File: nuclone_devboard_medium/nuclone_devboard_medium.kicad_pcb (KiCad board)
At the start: 2 copper layers, 50 x 76.2 mm, 40 parts, among them J1 JTAG_2X05, J2 TYPE-C-31-M-12, J3 nuclone_medium_left, J4 nuclone_medium_right, J5 Conn_02x06_Odd_Even, SW1 RESET, SW2 Bootloader, U1 MCP1702-3.3V, U2 TPESD0504C6

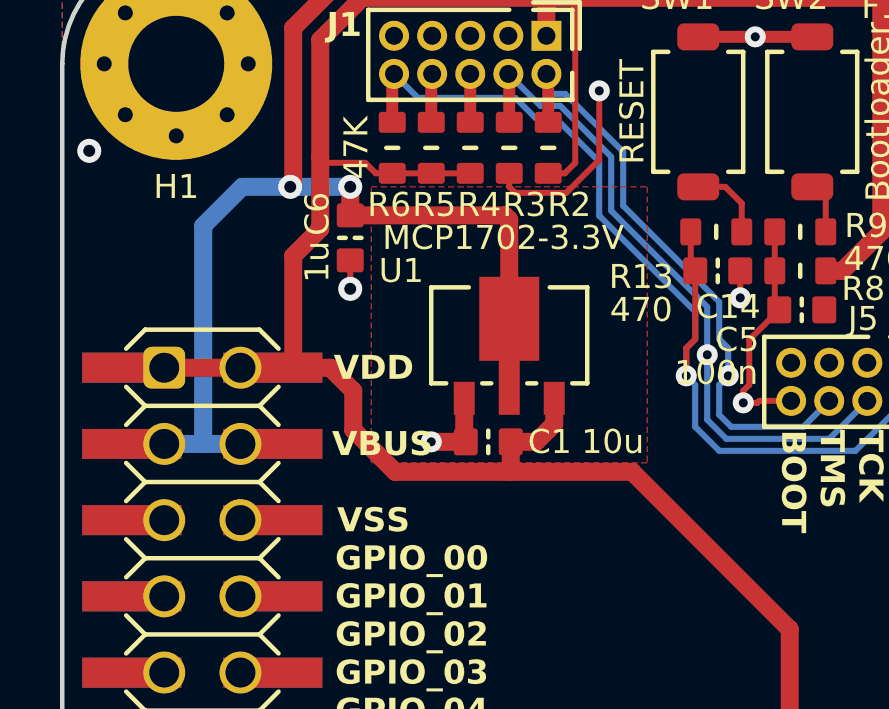
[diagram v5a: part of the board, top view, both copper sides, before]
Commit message: updated regulator cooling
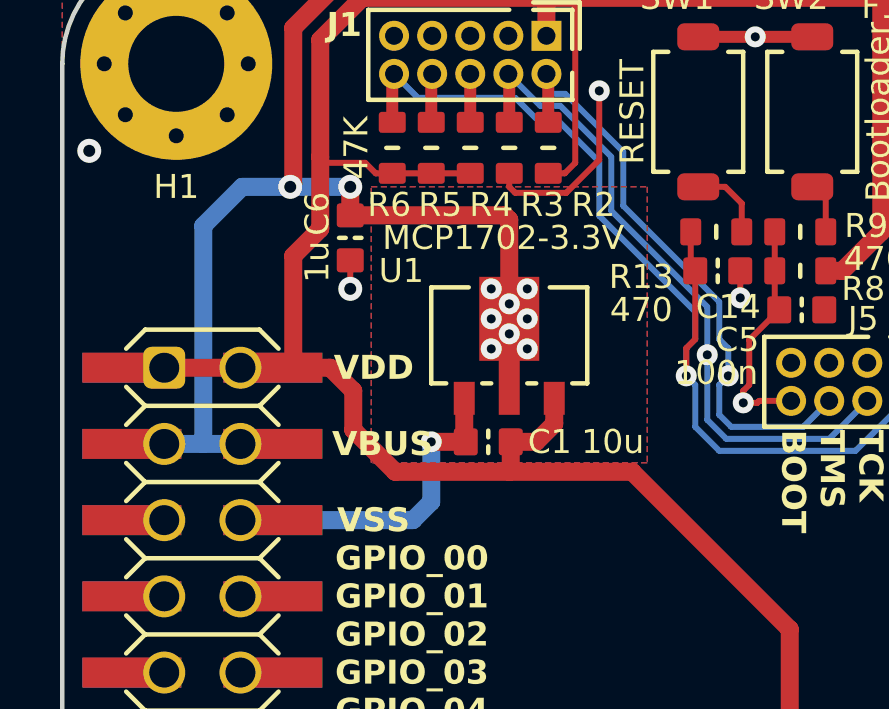
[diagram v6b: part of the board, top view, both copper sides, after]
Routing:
- net /VSS: track 36.0 -> 44.6 mm
- net /VBUS: track 89.4 -> 91.2 mm, vias 6 -> 14
- added copper zone on B.Cu, net /VBUS
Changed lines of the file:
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@@
     (property "ki_keywords" "R res resistor")
     (attr smd)
-    (fp_text reference "R3" (at 1.9 -0.5) (layer "F.SilkS")
+    (fp_text reference "R3" (at 1.9 -1.1) (layer "F.SilkS")
         (effects (font (size 0.8 0.8) (thickness 0.15)))
     )
@@
     (property "ki_keywords" "R res resistor")
     (attr smd)
-    (fp_text reference "R5" (at 1.9 -0.1) (layer "F.SilkS")
+    (fp_text reference "R5" (at 1.9 -0.3) (layer "F.SilkS")
         (effects (font (size 0.8 0.8) (thickness 0.15)))
     )
@@
     (property "ki_keywords" "R res resistor")
     (attr smd)
-    (fp_text reference "R2" (at 1.9 -0.7) (layer "F.SilkS")
+    (fp_text reference "R2" (at 1.9 -1.5) (layer "F.SilkS")
         (effects (font (size 0.8 0.8) (thickness 0.15)))
     )
@@
     (property "ki_keywords" "R res resistor")
     (attr smd)
-    (fp_text reference "R4" (at 1.9 -0.3) (layer "F.SilkS")
+    (fp_text reference "R4" (at 1.9 -0.7) (layer "F.SilkS")
         (effects (font (size 0.8 0.8) (thickness 0.15)))
     )
@@
     (style (thickness 0.1) (arrow_length 1.27) (text_position_mode 0) (extension_height 0.58642) (extension_offset 0.5) keep_text_aligned)
   )
-  (segment (start 69.7 69.85) (end 74.85 69.85) (width 0.6) (layer "F.Cu") (net 1))
   (segment (start 90.2 61.7) (end 90.3 61.8) (width 0.6) (layer "F.Cu") (net 1))
+  (segment (start 75 72.8) (end 75 72.9) (width 0.6) (layer "F.Cu") (net 1))
   (segment (start 69.7 61.7) (end 90.2 61.7) (width 0.6) (layer "F.Cu") (net 1))
+  (segment (start 75 73.8) (end 75 73.6) (width 0.6) (layer "F.Cu") (net 1))
   (segment (start 100.5 70.5) (end 101.7 69.3) (width 0.6) (layer "F.Cu") (net 1))
+  (segment (start 74.4 72.3) (end 74.9 72.8) (width 0.6) (layer "F.Cu") (net 1))
   (segment (start 67.8 68.8) (end 67.8 63.6) (width 0.6) (layer "F.Cu") (net 1))
   (segment (start 67.8 63.6) (end 69.7 61.7) (width 0.6) (layer "F.Cu") (net 1))
@@
   (segment (start 90.3 62.6) (end 89.85 63.05) (width 0.6) (layer "F.Cu") (net 1))
   (segment (start 89.85 64.5) (end 89.85 65.9) (width 0.6) (layer "F.Cu") (net 1))
+  (segment (start 74.4 73.3) (end 75 73.8) (width 0.6) (layer "F.Cu") (net 1))
   (segment (start 101.7 69.3) (end 101.7 62.4) (width 0.6) (layer "F.Cu") (net 1))
+  (segment (start 74.9 72.8) (end 75 72.8) (width 0.6) (layer "F.Cu") (net 1))
+  (segment (start 75 72.9) (end 75 72.9) (width 0.6) (layer "F.Cu") (net 1))
   (segment (start 97.577735 74.310961) (end 97.65 74.238696) (width 0.4) (layer "F.Cu") (net 1))
   (segment (start 90.3 61.8) (end 90.3 62.6) (width 0.6) (layer "F.Cu") (net 1))
+  (segment (start 74.85 69.85) (end 75 70) (width 0.6) (layer "F.Cu") (net 1))
+  (segment (start 69.7 69.85) (end 74.85 69.85) (width 0.6) (layer "F.Cu") (net 1))
   (segment (start 97.65 72.4) (end 97.55 72.3) (width 0.4) (layer "F.Cu") (net 1))
+  (segment (start 75 70) (end 75 72.8) (width 0.6) (layer "F.Cu") (net 1))
   (segment (start 89.85 63.05) (end 89.85 64.5) (width 0.6) (layer "F.Cu") (net 1))
   (segment (start 97.577735 74.310961) (end 97.566774 74.3) (width 0.4) (layer "F.Cu") (net 1))
-  (segment (start 74.85 69.85) (end 75 70) (width 0.6) (layer "F.Cu") (net 1))
+  (segment (start 75 72.9) (end 74.4 73.3) (width 0.6) (layer "F.Cu") (net 1))
   (segment (start 97.65 74.238696) (end 97.65 72.4) (width 0.4) (layer "F.Cu") (net 1))
   (segment (start 67.7 68.9) (end 67.8 68.8) (width 0.6) (layer "F.Cu") (net 1))
-  (segment (start 75 70) (end 75 73.6) (width 0.6) (layer "F.Cu") (net 1))
   (segment (start 69.7 68.9) (end 69.7 69.85) (width 0.6) (layer "F.Cu") (net 1))
   (segment (start 97.55 72.3) (end 96.92 72.3) (width 0.4) (layer "F.Cu") (net 1))
   (via (at 97.577735 74.310961) (size 0.7) (drill 0.3) (layers "F.Cu" "B.Cu") (net 1))
+  (via (at 75 72.8) (size 0.7) (drill 0.3) (layers "F.Cu" "B.Cu") (net 1))
+  (via (at 75 73.8) (size 0.7) (drill 0.3) (layers "F.Cu" "B.Cu") (net 1))
   (via (at 101.7 62.4) (size 0.8) (drill 0.4) (layers "F.Cu" "B.Cu") (net 1))
+  (via (at 74.4 72.3) (size 0.7) (drill 0.3) (layers "F.Cu" "B.Cu") (net 1))
   (via (at 90.3 61.8) (size 0.8) (drill 0.4) (layers "F.Cu" "B.Cu") (net 1))
+  (via (at 75.6 73.3) (size 0.7) (drill 0.3) (layers "F.Cu" "B.Cu") (net 1))
   (via (at 67.7 68.9) (size 0.8) (drill 0.4) (layers "F.Cu" "B.Cu") (net 1))
+  (via (at 75.6 74.3) (size 0.7) (drill 0.3) (layers "F.Cu" "B.Cu") (net 1))
+  (via (at 74.4 74.3) (size 0.7) (drill 0.3) (layers "F.Cu" "B.Cu") (net 1))
   (via (at 69.7 68.9) (size 0.8) (drill 0.4) (layers "F.Cu" "B.Cu") (net 1))
+  (via (at 75.6 72.3) (size 0.7) (drill 0.3) (layers "F.Cu" "B.Cu") (net 1))
   (via (at 100.5 70.5) (size 0.8) (drill 0.4) (layers "F.Cu" "B.Cu") (net 1))
+  (via (at 74.4 73.3) (size 0.7) (drill 0.3) (layers "F.Cu" "B.Cu") (net 1))
   (segment (start 67.7 68.9) (end 66.1 68.9) (width 0.6) (layer "B.Cu") (net 1))
   (segment (start 66.1 68.9) (end 64.8 70.2) (width 0.6) (layer "B.Cu") (net 1))
@@
   (via (at 88.4 69.6) (size 0.8) (drill 0.4) (layers "F.Cu" "B.Cu") (net 4))
   (via (at 72.4 77.4) (size 0.7) (drill 0.3) (layers "F.Cu" "B.Cu") (net 4))
+  (segment (start 72.4 79.4) (end 72.4 77.4) (width 0.6) (layer "B.Cu") (net 4))
+  (segment (start 71.79 80.01) (end 72.4 79.4) (width 0.6) (layer "B.Cu") (net 4))
+  (segment (start 66.04 80.01) (end 71.79 80.01) (width 0.6) (layer "B.Cu") (net 4))
   (segment (start 106.5 70.05) (end 108 70.05) (width 0.2) (layer "F.Cu") (net 5))
   (segment (start 76.3 65.195) (end 76.24 65.135) (width 0.4) (layer "F.Cu") (net 14))
@@
   (segment (start 85.1 68.9) (end 85.5 68.9) (width 0.2) (layer "F.Cu") (net 85))
   (segment (start 85.55 68.95) (end 85.55 70.4) (width 0.2) (layer "F.Cu") (net 85))
-  (zone (net 1) (net_name "/VBUS") (layer "F.Cu") (hatch edge 0.508)
-    (priority 1)
-    (connect_pads (clearance 0.3))
-    (min_thickness 0.2) (filled_areas_thickness no)
-    (fill yes (thermal_gap 0.2) (thermal_bridge_width 0.4))
-    (polygon
-      (pts
-        (xy 79.6 68.9)
-        (xy 79.6 78.1)
-        (xy 70.4 78.1)
-        (xy 70.4 68.9)
-      )
-    )
-  )
   (zone (net 4) (net_name "/VSS") (layer "F.Cu") (hatch edge 0.508)
     (connect_pads (clearance 0.3))
@@
       )
     )
+  )
+  (zone (net 1) (net_name "/VBUS") (layers "F&B.Cu") (hatch edge 0.508)
+    (priority 1)
+    (connect_pads (clearance 0.3))
+    (min_thickness 0.2) (filled_areas_thickness no)
+    (fill yes (thermal_gap 0.2) (thermal_bridge_width 0.4))
+    (polygon
+      (pts
+        (xy 79.6 68.9)
+        (xy 79.6 78.1)
+        (xy 70.4 78.1)
+        (xy 70.4 68.9)
+      )
+    )

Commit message: updated versionnumbers
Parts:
- N2: value 20240107 -> V20240114; footprint SquantorLabels:Label_version -> SquantorLabels:Label_Generic
- N4: value NuClone Medium template V1.2 -> NuClone Medium template V1.3
- N5: value Nuclone Template 20240107 -> Nuclone Template V20240114
- moved N2 1.45 mm to (84.9, 134.0), turned to 180 degrees
- moved N3 0.97 mm to (84.9, 135.6)
- moved N4 0.73 mm to (84.9, 135.8)
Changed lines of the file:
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@@
   )
   (footprint "SquantorLabels:Label_Generic" (layer "F.Cu")
-    (at 85.5 136.2)
+    (at 84.9 135.7875)
     (descr "Label for general purpose use")
     (tags "Label")
@@
         (effects (font (size 1 1) (thickness 0.15)))
     )
-    (fp_text value "NuClone Medium template V1.2" (at 0.8 -0.1) (layer "F.SilkS")
+    (fp_text value "NuClone Medium template V1.3" (at 0 0.0125) (layer "F.SilkS")
         (effects (font (size 0.8 0.8) (thickness 0.15)))
     )
@@
     )
   )
-  (footprint "SquantorLabels:Label_version" (layer "B.Cu")
-    (at 83.45 134.05)
+  (footprint "SquantorLabels:Label_Generic" (layer "B.Cu")
+    (at 84.9 133.9875 180)
+    (descr "Label for general purpose use")
+    (tags "Label")
     (property "Sheetfile" "nuclone_devboard_medium.kicad_sch")
     (property "Sheetname" "")
-    (attr through_hole)
-    (fp_text reference "N2" (at 0 -1.4 180) (layer "B.Fab") hide
+    (attr smd)
+    (fp_text reference "N2" (at 0 -1.85) (layer "B.Fab") hide
         (effects (font (size 1 1) (thickness 0.15)) (justify mirror))
     )
-    (fp_text value "20240107" (at 0.8 0.1 180) (layer "B.SilkS")
-        (effects (font (size 1 1) (thickness 0.15)) (justify mirror))
-    )
-    (fp_text user "V:" (at -4.9 0.1 180) (layer "B.SilkS")
-        (effects (font (size 1 1) (thickness 0.15)) (justify mirror))
-    )
+    (fp_text value "V20240114" (at -0.05 0.1) (layer "B.SilkS")
+        (effects (font (size 0.8 0.8) (thickness 0.15)) (justify mirror))
+    )
+    (fp_line (start -0.5 -0.6) (end 0.5 -0.6)
+      (stroke (width 0.15) (type solid)) (layer "B.SilkS"))
   )
   (footprint "Symbol:OSHW-Symbol_6.7x6mm_SilkScreen" (layer "B.Cu")
-    (at 84.95 130.05 180)
+    (at 85 130.05 180)
     (descr "Open Source Hardware Symbol")
     (tags "Logo Symbol OSHW")
@@
   )
   (footprint "SquantorLabels:Label_Generic" (layer "B.Cu")
-    (at 85.75 136.05 180)
+    (at 84.9 135.5875 180)
     (descr "Label for general purpose use")
     (tags "Label")
@@
         (effects (font (size 1 1) (thickness 0.15)) (justify mirror))
     )
-    (fp_text value "JLCJLCJLCJLC" (at 0.8 0.1) (layer "B.SilkS")
+    (fp_text value "JLCJLCJLCJLC" (at 0 -0.0125) (layer "B.SilkS")
         (effects (font (size 0.8 0.8) (thickness 0.15)) (justify mirror))
     )
@@
         (effects (font (size 1 1) (thickness 0.15)) (justify mirror))
     )
-    (fp_text value "Nuclone Template 20240107" (at 0.8 0.23) (layer "B.SilkS")
+    (fp_text value "Nuclone Template V20240114" (at 0.8 0.23) (layer "B.SilkS")
         (effects (font (size 0.8 0.8) (thickness 0.15)) (justify mirror))
     )
